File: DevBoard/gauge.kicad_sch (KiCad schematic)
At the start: 59 parts, among them J101 Pack (welded 4S) - use instea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, J102 Cell 1 NTC 10k 103AT, J103 EV2400 SMBus, J104 Bench PACK_P, J105 Cell 2 NTC 10k 103AT, J106 Cell 3 NTC 10k 103AT, J107 Cell 4 NTC 10k 103AT, Q101 AGM404AP1, Q102 AGM404AP1, Q103 BSS138, SW101 WAKE, U101 BQ40Z50RSMR-R2

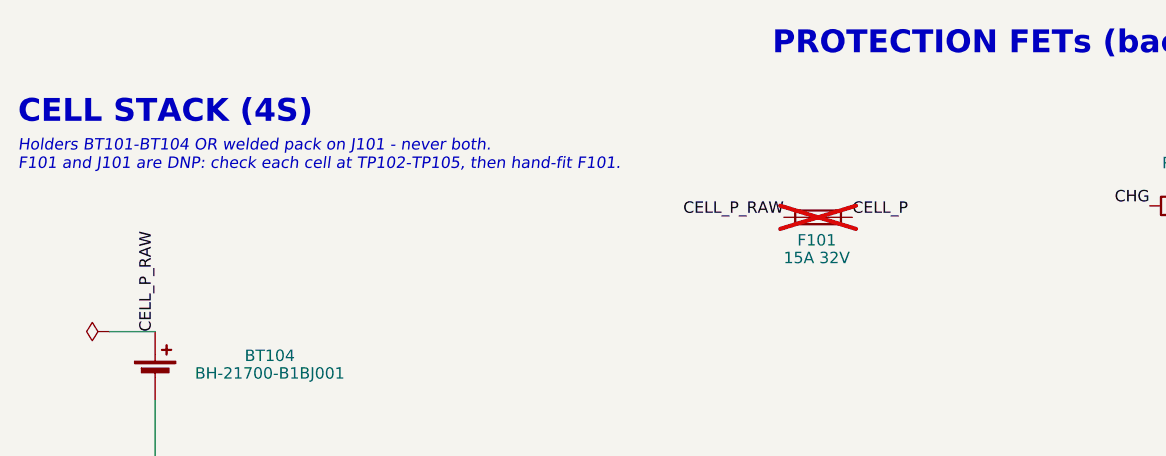
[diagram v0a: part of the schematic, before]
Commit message: Dev board: F101 JLC-placed again; check cells before waking the gauge
Hand-fitting F101 meant soldering beside an installed 16.8 V stack with no
fuse, and since the BAT feed moved before F101 it no longer isolated the
gauge either. The loads sit behind Q101/Q102, which stay off on a fresh
gauge (FET_EN off), so the cell check moves to before the gauge is woken:
insert cells, check TP102-TP105 and TP108, then wake and configure.

Co-Authored-By: Claude Opus 5.5 <noreply@anthropic.com>
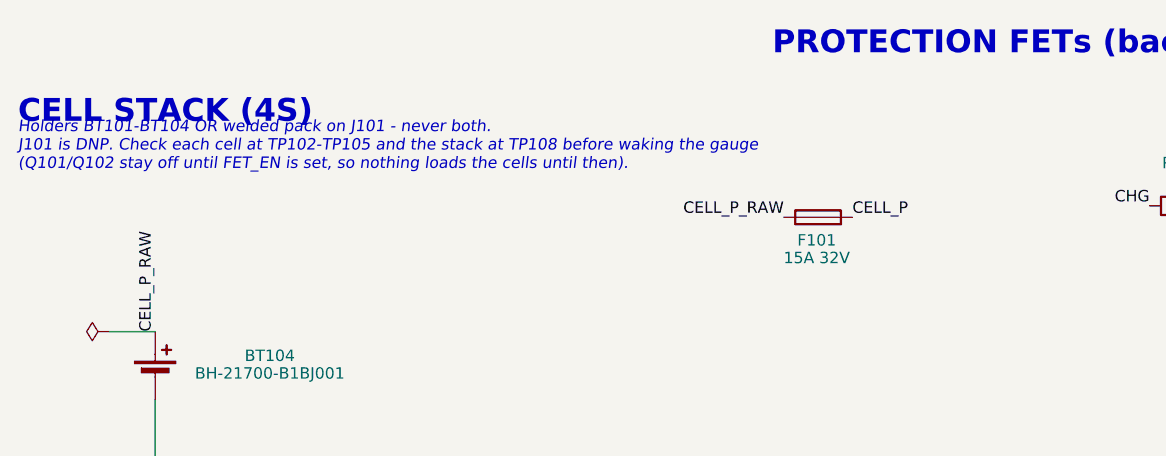
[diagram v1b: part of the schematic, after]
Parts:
- F101: Notes Hand-fit after checking all four cells at TP102-TP105 (JLC 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 -> JLC-placed (rev A5; was DNP/hand-fit). 15 A for 100 W out a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; now fitted
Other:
- note added: "Holders BT101-BT104 OR welded pack on J101 - never both. J101 is DNP. Check each cell at TP102-TP105 and the stack at TP108 before waking the gauge (Q101/Q102 stay off until FET_EN is set, so nothing loads the cells until then)."
- note removed: "Holders BT101-BT104 OR welded pack on J101 - never both. F101 and J101 are DNP: check each cell at TP102-TP105, then hand-fit F101."
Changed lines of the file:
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@@
 		)
 	)
-	(text "Holders BT101-BT104 OR welded pack on J101 - never both.\nF101 and J101 are DNP: check each cell at TP102-TP105, then hand-fit F101."
+	(text "Holders BT101-BT104 OR welded pack on J101 - never both.\nJ101 is DNP. Check each cell at TP102-TP105 and the stack at TP108 before waking the gauge\n(Q101/Q102 stay off until FET_EN is set, so nothing loads the cells until then)."
 		(exclude_from_sim no)
 		(at 22.86 40.64 0)
@@
 		(on_board yes)
 		(in_pos_files yes)
-		(dnp yes)
+		(dnp no)
 		(property "Reference" "F101"
 			(at 111.61 48.27 90)
@@
 			)
 		)
-		(property "Notes" "Hand-fit after checking all four cells at TP102-TP105 (JLC leaves it off). 15 A for 100 W out at the 12 V low end (~10 A continuous, 75 % derating). Interrupt 300 A at 24 Vdc (pack max 16.8 V). 3.9 mOhm: 0.4 W at 10 A, give it copper. Review 2 D3: 15 A holds only if the gauge cut-off under load stays at 2.8 V/cell or higher (9.8 A at 100 W); a lower cut-off needs 1206FA-20A"
+		(property "Notes" "JLC-placed (rev A5; was DNP/hand-fit). 15 A for 100 W out at the 12 V low end (~10 A continuous, 75 % derating). Interrupt 300 A at 24 Vdc (pack max 16.8 V). 3.9 mOhm: 0.4 W at 10 A, give it copper. Review 2 D3: 15 A holds only if the gauge cut-off under load stays at 2.8 V/cell or higher (9.8 A at 100 W); a lower cut-off needs 1206FA-20A"
 			(at 0 0 0)
 			(hide yes)

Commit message: Dev board: SMD test loops (RH-S2761-46R) instead of Keystone through-hole
All 45 loop test points become ronghe RH-S2761-46R (LCSC C55121754), the
JLC-stocked equivalent of the Harwin S2761-46R: 1.6 x 0.8 x 1.15 mm SMT
loop on an 0603 land pattern, 3.5 A. New footprint
MonolithDev:TestPoint_Harwin_S2761_0603 (make_footprints.py section 11),
both pads pin 1 and jumpered. JLC places them; no through-hole assembly.

Co-Authored-By: Claude Opus 5.5 <noreply@anthropic.com>
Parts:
- TP101, TP102, TP103, TP104, TP105, TP106, TP107, TP108, TP109: footprint TestPoint:TestPoint_Keystone_5000-5004_Miniature -> MonolithDev:TestPoint_Harwin_S2761_0603; LCSC (none) -> C55121754; MPN (none) -> RH-S2761-46R (ronghe; Harwin S2761-46R equivalent)
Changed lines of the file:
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@@
 			)
 		)
-		(property "Footprint" "TestPoint:TestPoint_Keystone_5000-5004_Miniature"
+		(property "Footprint" "MonolithDev:TestPoint_Harwin_S2761_0603"
 			(at 96.52 264.16 0)
 			(hide yes)
@@
 			)
 		)
+		(property "LCSC" "C55121754"
+			(at 91.44 264.16 0)
+			(hide yes)
+			(show_name no)
+			(do_not_autoplace no)
+			(effects
+				(font
+					(size 1.27 1.27)
+				)
+			)
+		)
+		(property "MPN" "RH-S2761-46R (ronghe; Harwin S2761-46R equivalent)"
+			(at 91.44 264.16 0)
+			(hide yes)
+			(show_name no)
+			(do_not_autoplace no)
+			(effects
+				(font
+					(size 1.27 1.27)
+				)
+			)
+		)
 		(pin "1"
 		)
@@
 			)
 		)
-		(property "Footprint" "TestPoint:TestPoint_Keystone_5000-5004_Miniature"
+		(property "Footprint" "MonolithDev:TestPoint_Harwin_S2761_0603"
 			(at 271.78 50.8 0)
 			(hide yes)
@@
 			)
 		)
+		(property "LCSC" "C55121754"
+			(at 266.7 50.8 0)
+			(hide yes)
+			(show_name no)
+			(do_not_autoplace no)
+			(effects
+				(font
+					(size 1.27 1.27)
+				)
+			)
+		)
+		(property "MPN" "RH-S2761-46R (ronghe; Harwin S2761-46R equivalent)"
+			(at 266.7 50.8 0)
+			(hide yes)
+			(show_name no)
+			(do_not_autoplace no)
+			(effects
+				(font
+					(size 1.27 1.27)
+				)
+			)
+		)
 		(pin "1"
 		)
@@
 			)
 		)
-		(property "Footprint" "TestPoint:TestPoint_Keystone_5000-5004_Miniature"
+		(property "Footprint" "MonolithDev:TestPoint_Harwin_S2761_0603"
 			(at 81.28 264.16 0)
 			(hide yes)
@@
 			)
 		)
+		(property "LCSC" "C55121754"
+			(at 76.2 264.16 0)
+			(hide yes)
+			(show_name no)
+			(do_not_autoplace no)
+			(effects
+				(font
+					(size 1.27 1.27)
+				)
+			)
+		)
+		(property "MPN" "RH-S2761-46R (ronghe; Harwin S2761-46R equivalent)"
+			(at 76.2 264.16 0)
+			(hide yes)
+			(show_name no)
+			(do_not_autoplace no)
+			(effects
+				(font
+					(size 1.27 1.27)
+				)
+			)
+		)
 		(pin "1"
 		)
@@
 			)
 		)
-		(property "Footprint" "TestPoint:TestPoint_Keystone_5000-5004_Miniature"
+		(property "Footprint" "MonolithDev:TestPoint_Harwin_S2761_0603"
 			(at 50.8 264.16 0)
 			(hide yes)
@@
 			)
 		)
+		(property "LCSC" "C55121754"
+			(at 45.72 264.16 0)
+			(hide yes)
+			(show_name no)
+			(do_not_autoplace no)
+			(effects
+				(font
+					(size 1.27 1.27)
+				)
+			)
+		)
+		(property "MPN" "RH-S2761-46R (ronghe; Harwin S2761-46R equivalent)"
+			(at 45.72 264.16 0)
+			(hide yes)
+			(show_name no)
+			(do_not_autoplace no)
+			(effects
+				(font
+					(size 1.27 1.27)
+				)
+			)
+		)
 		(pin "1"
 		)
@@
 			)
 		)
-		(property "Footprint" "TestPoint:TestPoint_Keystone_5000-5004_Miniature"
+		(property "Footprint" "MonolithDev:TestPoint_Harwin_S2761_0603"
 			(at 111.76 264.16 0)
 			(hide yes)
@@
 			)
 		)
+		(property "LCSC" "C55121754"
+			(at 106.68 264.16 0)
+			(hide yes)
+			(show_name no)
+			(do_not_autoplace no)
+			(effects
+				(font
+					(size 1.27 1.27)
+				)
+			)
+		)
+		(property "MPN" "RH-S2761-46R (ronghe; Harwin S2761-46R equivalent)"
+			(at 106.68 264.16 0)
+			(hide yes)
+			(show_name no)
+			(do_not_autoplace no)
+			(effects
+				(font
+					(size 1.27 1.27)
+				)
+			)
+		)
 		(pin "1"
 		)
@@
 			)
 		)
-		(property "Footprint" "TestPoint:TestPoint_Keystone_5000-5004_Miniature"
+		(property "Footprint" "MonolithDev:TestPoint_Harwin_S2761_0603"
 			(at 66.04 264.16 0)
 			(hide yes)
@@
 			)
 		)
+		(property "LCSC" "C55121754"
+			(at 60.96 264.16 0)
+			(hide yes)
+			(show_name no)
+			(do_not_autoplace no)
+			(effects
+				(font
+					(size 1.27 1.27)
+				)
+			)
+		)
+		(property "MPN" "RH-S2761-46R (ronghe; Harwin S2761-46R equivalent)"
+			(at 60.96 264.16 0)
+			(hide yes)
+			(show_name no)
+			(do_not_autoplace no)
+			(effects
+				(font
+					(size 1.27 1.27)
+				)
+			)
+		)
 		(pin "1"
 		)
@@
 			)
 		)
-		(property "Footprint" "TestPoint:TestPoint_Keystone_5000-5004_Miniature"
+		(property "Footprint" "MonolithDev:TestPoint_Harwin_S2761_0603"
 			(at 317.5 190.5 0)
 			(hide yes)
@@
 			)
 		)
+		(property "LCSC" "C55121754"
+			(at 312.42 190.5 0)
+			(hide yes)
+			(show_name no)
+			(do_not_autoplace no)
+			(effects
+				(font
+					(size 1.27 1.27)
+				)
+			)
+		)
+		(property "MPN" "RH-S2761-46R (ronghe; Harwin S2761-46R equivalent)"
+			(at 312.42 190.5 0)
+			(hide yes)
+			(show_name no)
+			(do_not_autoplace no)
+			(effects
+				(font
+					(size 1.27 1.27)
+				)
+			)
+		)
 		(pin "1"
 		)
@@
 			)
 		)
-		(property "Footprint" "TestPoint:TestPoint_Keystone_5000-5004_Miniature"
+		(property "Footprint" "MonolithDev:TestPoint_Harwin_S2761_0603"
 			(at 121.92 264.16 0)
 			(hide yes)
@@
 			)
 		)
+		(property "LCSC" "C55121754"
+			(at 121.92 264.16 0)
+			(hide yes)
+			(show_name no)
+			(do_not_autoplace no)
+			(effects
+				(font
+					(size 1.27 1.27)
+				)
+			)
+		)
+		(property "MPN" "RH-S2761-46R (ronghe; Harwin S2761-46R equivalent)"
+			(at 121.92 264.16 0)
+			(hide yes)
+			(show_name no)
+			(do_not_autoplace no)
+			(effects
+				(font
+					(size 1.27 1.27)
+				)
+			)
+		)
 		(pin "1"
 		)
@@
 			)
 		)
-		(property "Footprint" "TestPoint:TestPoint_Keystone_5000-5004_Miniature"
+		(property "Footprint" "MonolithDev:TestPoint_Harwin_S2761_0603"
 			(at 137.16 264.16 0)
 			(hide yes)
@@
 			(at 137.16 264.16 0)
 			(hide yes)
+			(show_name no)
+			(do_not_autoplace no)
+			(effects
+				(font
+					(size 1.27 1.27)
+				)
+			)
+		)
+		(property "LCSC" "C55121754"
+			(at 137.16 264.16 0)
+			(hide yes)
+			(show_name no)
+			(do_not_autoplace no)
+			(effects
+				(font
+					(size 1.27 1.27)
+				)
+			)
+		)
+		(property "MPN" "RH-S2761-46R (ronghe; Harwin S2761-46R equivalent)"
+			(at 137.16 264.16 0)
+			(hide yes)
